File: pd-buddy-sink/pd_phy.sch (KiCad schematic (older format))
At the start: 5 parts, among them U3 FUSB302BMPX

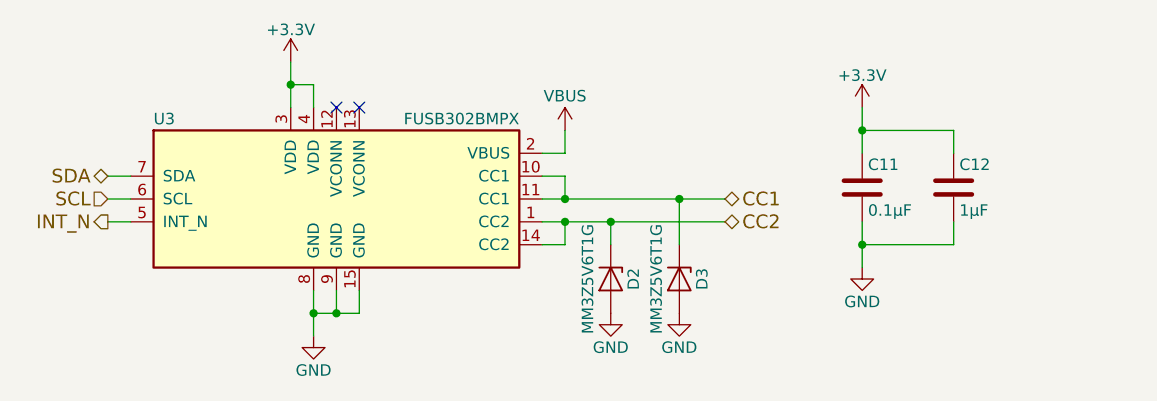
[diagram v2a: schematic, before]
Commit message: Update to KiCad 5.0 nightly
Hooray, new stuff!  The STM32 symbol is a reasonable size now!  We have
a sym-lib-table!  Everything is great, and I'm excited!

The board's a bit of a mess though, as the silkscreen needs to be laid
out nicely.  Oh well, details.
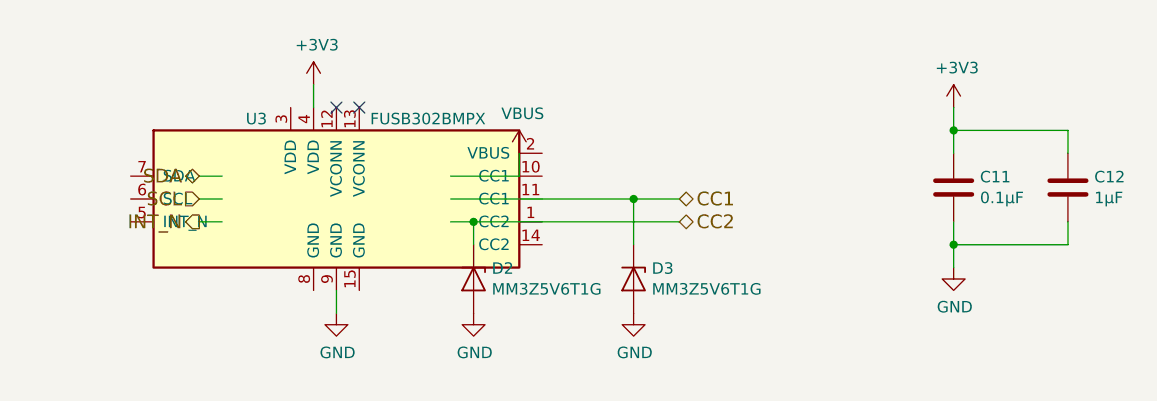
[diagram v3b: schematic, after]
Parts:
- removed C11: 0.1μF, Capacitors_SMD:C_0402, symbol C
- removed C12: 1μF, Capacitors_SMD:C_0402, symbol C
- removed D2, D3: MM3Z5V6T1G, Diodes_SMD:D_SOD-323, symbol D_Zener
- removed U3: FUSB302BMPX, Housings_DFN_QFN:Fairchild_MLP14D, symbol FUSB302BMPX
- added C11: 0.1μF, Capacitor_SMD:C_0402_1005Metric, symbol Device:C
- added C12: 1μF, Capacitor_SMD:C_0402_1005Metric, symbol Device:C
- added D2, D3: MM3Z5V6T1G, Diode_SMD:D_SOD-323, symbol Device:D_Zener
- added U3: FUSB302BMPX, Package_DFN_QFN:WQFN-14-1EP_2.5x2.5mm_P0.5mm_EP1.45x1.45mm, symbol Interface_USB:FUSB302BMPX
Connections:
- net labels added: +3V3
- net labels removed: +3.3V
- wire segments 26 -> 21
